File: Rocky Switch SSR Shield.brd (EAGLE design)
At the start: 69.6 x 47.6 mm, 25 parts

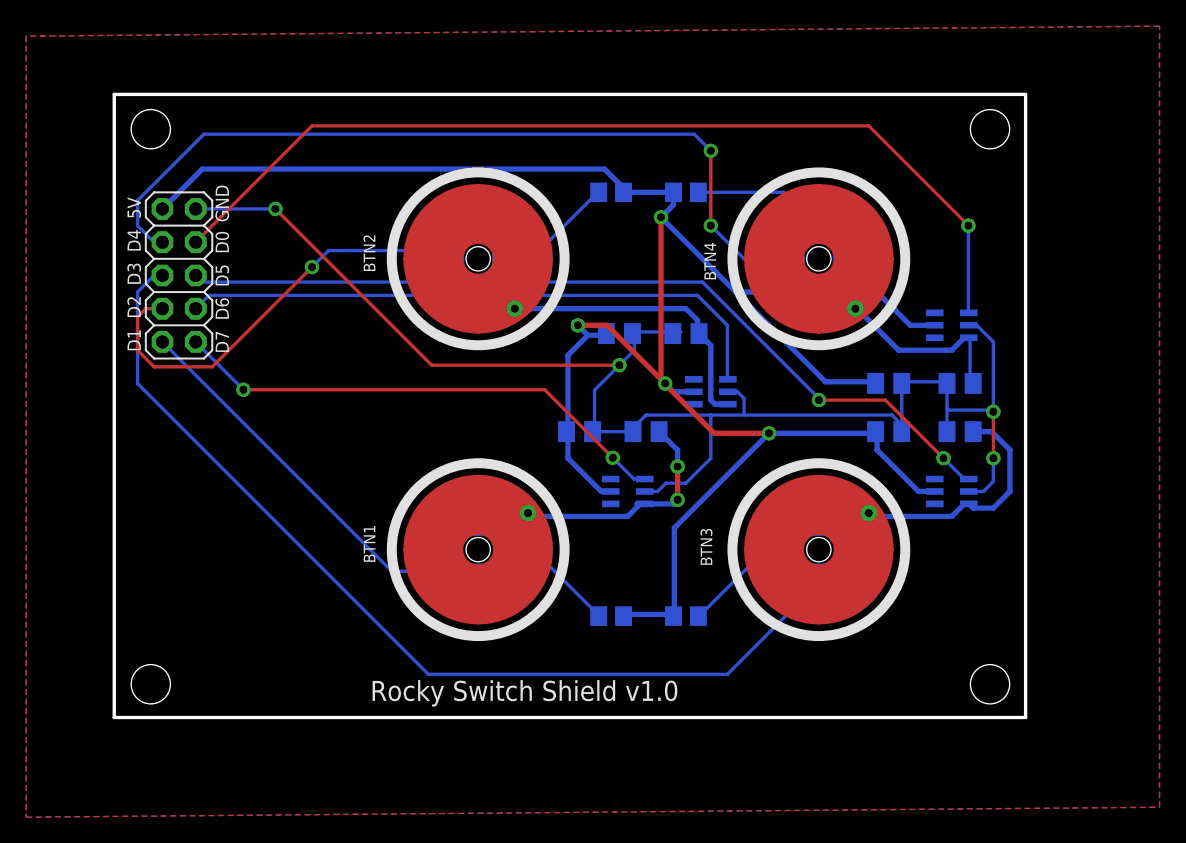
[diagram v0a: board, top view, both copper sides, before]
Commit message: Add shield for rocky relay
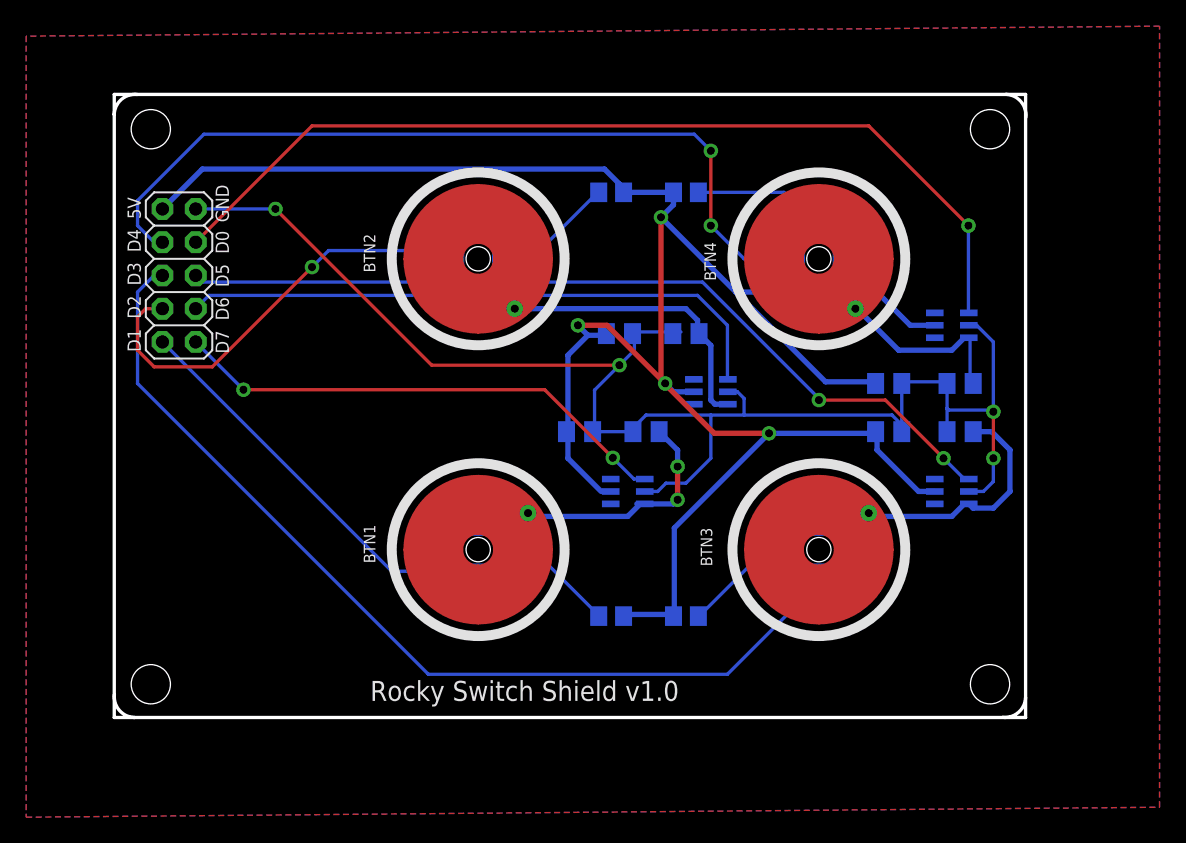
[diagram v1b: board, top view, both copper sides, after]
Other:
- board size 69.6 x 47.6 mm -> 69.7 x 47.6 mm
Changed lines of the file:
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@@
 <?xml version="1.0" encoding="utf-8"?>
 <!DOCTYPE eagle SYSTEM "eagle.dtd">
-<eagle version="7.6.0">
+<eagle version="8.2.1">
 <drawing>
 <settings>
@@
 <setting verticaltext="up"/>
 </settings>
-<grid distance="25" unitdist="mil" unit="mil" style="lines" multiple="1" display="no" altdistance="5" altunitdist="mil" altunit="mil"/>
+<grid distance="1" unitdist="mil" unit="mil" style="lines" multiple="1" display="no" altdistance="5" altunitdist="mil" altunit="mil"/>
 <layers>
 <layer number="1" name="Top" color="4" fill="1" visible="yes" active="yes"/>
@@
 <board>
 <plain>
-<wire x1="2.667" y1="4.318" x2="72.314" y2="4.318" width="0.254" layer="20"/>
+<wire x1="2.667" y1="4.318" x2="4.2037" y2="4.318" width="0.254" layer="20"/>
+<wire x1="4.2037" y1="4.318" x2="72.314" y2="4.318" width="0.254" layer="20"/>
 <wire x1="72.314" y1="4.318" x2="72.314" y2="51.933" width="0.254" layer="20"/>
 <wire x1="72.314" y1="51.933" x2="2.667" y2="51.933" width="0.254" layer="20"/>
-<wire x1="2.667" y1="51.933" x2="2.667" y2="4.318" width="0.254" layer="20"/>
+<wire x1="2.667" y1="51.933" x2="2.667" y2="50.4063" width="0.254" layer="20"/>
 <text x="11.43" y="42.164" size="1.016" layer="25" font="vector" ratio="15" rot="SR90">GND</text>
 <text x="11.43" y="32.131" size="1.016" layer="25" font="vector" ratio="15" rot="SR90">D7</text>
@@
 <circle x="68.072" y="36.195" radius="0.283978125" width="0.4064" layer="22"/>
 <circle x="49.53" y="31.242" radius="0.283978125" width="0.4064" layer="22"/>
+<wire x1="2.667" y1="50.4063" x2="2.667" y2="4.318" width="0.254" layer="20"/>
+<wire x1="70.8025" y1="51.943" x2="72.3265" y2="50.1777" width="0.254" layer="20" curve="-94.552163"/>
+<wire x1="2.667" y1="50.4063" x2="4.4323" y2="51.9303" width="0.254" layer="20" curve="-94.552163"/>
+<wire x1="4.2037" y1="4.318" x2="2.6797" y2="6.0833" width="0.254" layer="20" curve="-94.552163"/>
+<wire x1="72.3138" y1="5.8547" x2="70.5485" y2="4.3307" width="0.254" layer="20" curve="-94.552163"/>
 </plain>
 <attributes>
